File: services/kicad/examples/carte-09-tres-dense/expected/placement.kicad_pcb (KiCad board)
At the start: 2 copper layers, 130 x 100 mm, 62 parts, among them J1 IN_5V, J10 IO0, J11 IO1, J12 IO2, J13 IO3, J14 IO4, J2 SWD, U1 STM32F103C8T6, U2 AMS1117-3.3

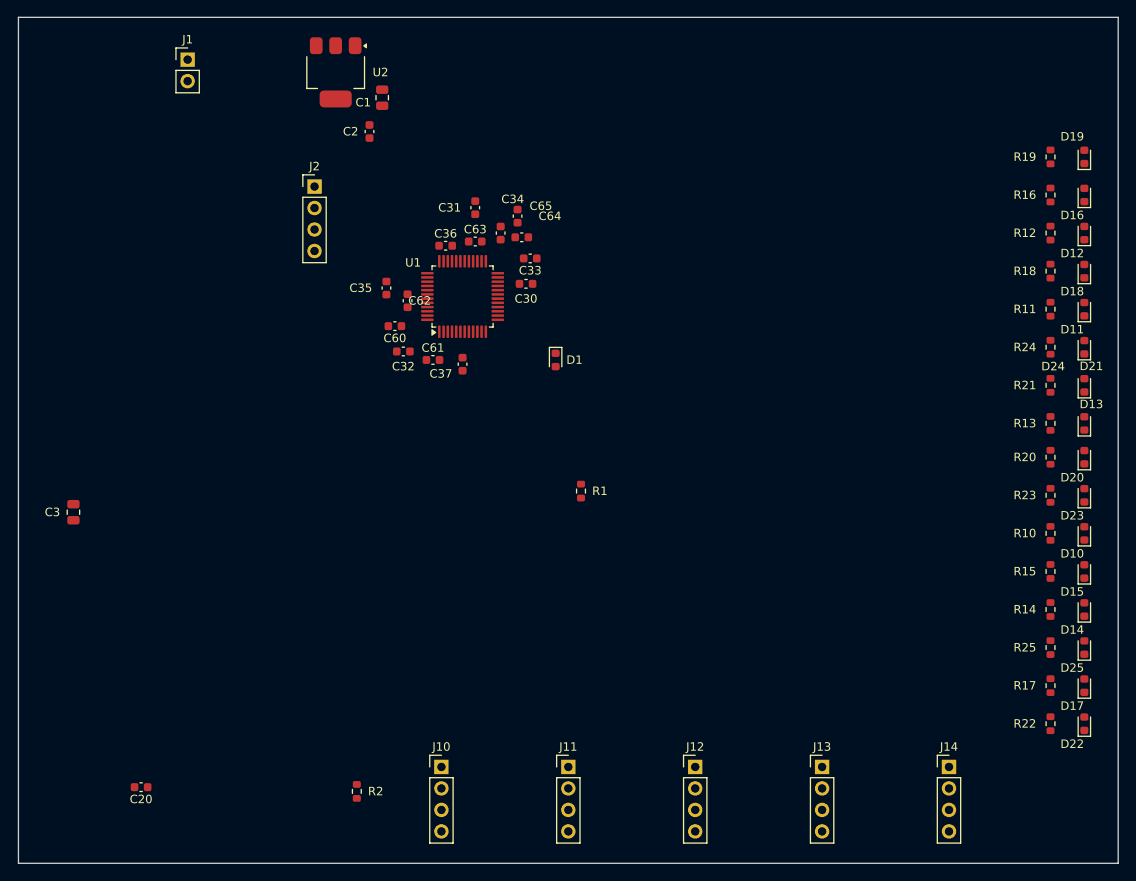
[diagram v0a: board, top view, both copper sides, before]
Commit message: feat(placement): les peripheriques se REPARTISSENT, ils ne s empilent plus
Question de l utilisateur devant le rendu : « c est quoi ce type de placement ? ».
Les composants s entassaient d un seul cote du boitier, etiquettes de
serigraphie l une sur l autre, trois quarts de la couronne vides.

TROIS CAUSES, toutes dans `_poser_les_peripheriques`, toutes la meme faute —
un angle unique pour tout un groupe :

  - les DIRECTS qui visent la meme broche (tous les decouplages d un rail,
    toutes les resistances d un meme signal) recevaient le MEME `angle_vers`
    et le meme rayon de depart ;
  - les SUIVEURS d un meme parent recevaient tous atan2(parent - centre) ;
  - les ISOLES partaient tous de l angle 0.0, c est-a-dire du meme point.

`le_long_du_rayon` ne s ecartait qu une fois la place prise : d ou la file.

REMEDE : `_ecart_en_eventail`. Le PREMIER de chaque groupe garde EXACTEMENT la
direction calculee — c est la topologie, on ne la perd pas pour faire joli — et
les suivants s ecartent symetriquement de 3 x `_PAS_ANGLE_DEG`.
Rien de deja pose ne bouge : seul l ANGLE DE DEPART de la recherche change, et
`le_long_du_rayon` reste seul juge de ce qui est libre.

BANC DES DIX CARTES, contour resserre ET peripheriques repartis :

    carte             demandee    livree         err  manq
    carte-01           25 x 20    20,1 x 13,6     0    0
    carte-02           55 x 40    34,9 x 25,2     0    0
    carte-03           50 x 35    27,6 x 19,9     0    0
    carte-04           60 x 45    36,6 x 29,8     0    0
    carte-05           70 x 50    40,0 x 32,6     0    0
    carte-06           80 x 60    46,5 x 36,4     0    0
    carte-07          110 x 80    47,7 x 38,8     0    0
    carte-08          125 x 95    57,4 x 44,1     0    0
    carte-09          130 x 100   57,8 x 45,2     0    0
    carte-10          140 x 105   59,0 x 45,8     0    0

Dix sur dix, 100 % route. carte-07 gagne 5,5 mm de largeur sur le passage
precedent, carte-06 deux, carte-10 deux. Sur ca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
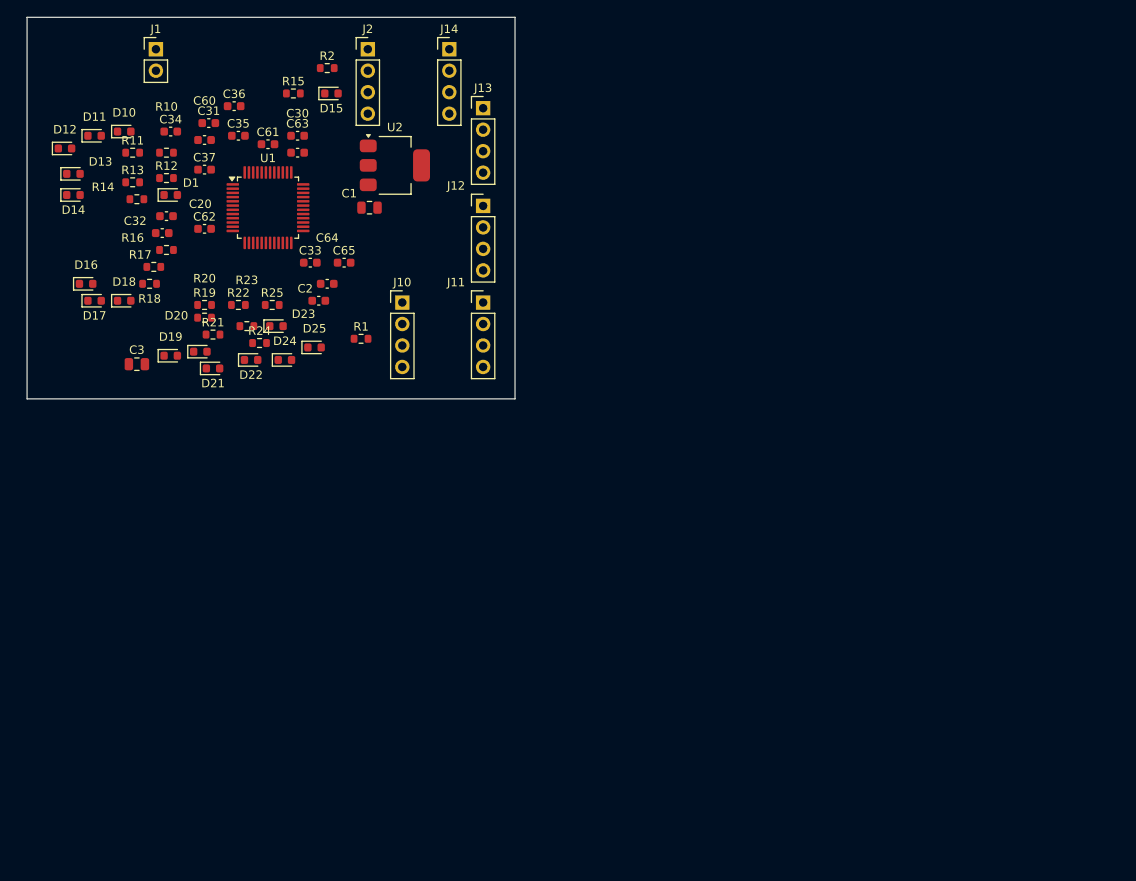
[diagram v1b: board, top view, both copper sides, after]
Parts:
- moved D14 129.2 mm to (90.0, 76.0), turned to 0 degrees
- moved D17 125.5 mm to (92.5, 88.5), turned to 0 degrees
- moved D13 123.1 mm to (90.0, 73.5), turned to 0 degrees
- moved D10 123.0 mm to (96.0, 68.5), turned to 0 degrees
- moved D12 120.9 mm to (89.0, 70.5), turned to 0 degrees
- moved D11 118.8 mm to (92.5, 69.0), turned to 0 degrees
- moved D16 118.5 mm to (91.5, 86.5), turned to 0 degrees
- moved R14 118.4 mm to (97.5, 76.5), turned to 0 degrees
- moved R17 117.0 mm to (99.5, 84.5), turned to 0 degrees
- moved R10 113.8 mm to (101.0, 71.0), turned to 0 degrees
- moved D18 113.6 mm to (96.0, 88.5), turned to 0 degrees
- moved R13 112.2 mm to (97.0, 74.5), turned to 0 degrees
- moved D19 110.5 mm to (101.5, 95.0), turned to 0 degrees
- moved R11 110.1 mm to (97.0, 71.0), turned to 0 degrees
- moved R22 108.0 mm to (109.5, 89.0), turned to 0 degrees
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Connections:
- U1 pad 36: Net-(U1-36) -> PWR_FLAG
- U1 pad 48: Net-(U1-48) -> PWR_FLAG
- U1 pad 9: IO_L5 -> PWR_FLAG
- U2 pad 3: VIN -> PWR_FLAG
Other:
- board size 130 x 100 mm -> 57.7 x 45.1 mm

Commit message: docs(banc): les dix boards du banc du 2026-09-23, service corrige
Artefacts du banc dont le tableau est deja commite : les dix cartes a
100 % route, 0 erreur, 0 connexion manquante, chacune a la taille de son
circuit.

Co-Authored-By: Claude Opus 5 <noreply@anthropic.com>
Claude-Session: https://claude.ai/code/session_01TnMqm4La2CxQHHB5K8aSSV
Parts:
- moved C36 15.0 mm to (105.0, 80.0)
- moved C34 14.1 mm to (105.5, 82.0)
- moved C63 13.2 mm to (103.5, 67.0)
- moved C32 11.5 mm to (101.0, 69.0)
- moved C31 10.6 mm to (116.0, 71.0)
- moved C62 10.5 mm to (105.5, 69.5)
- moved C64 9.51 mm to (110.5, 86.0)
- moved C30 3.64 mm to (113.0, 70.0)
- moved C60 3.64 mm to (109.0, 68.5)
- moved C65 3.20 mm to (120.0, 86.5)
- moved C35 3.04 mm to (110.0, 66.0)
- moved C61 2.06 mm to (112.5, 68.0)
- moved J12 1.00 mm to (138.4, 76.3)
- moved J13 1.00 mm to (138.4, 64.7)
- moved J11 0.87 mm to (138.4, 87.8)
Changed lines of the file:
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@@
 		(generator "kicad-footprint-generator")
 		(layer "F.Cu")
-		(at 116.5 71)
+		(at 113 70)
 		(descr "Capacitor SMD 0603 (1608 Metric), square (rectangular) end terminal, IPC-7351 nominal, (Body size source: IPC-SM-782 page 76, https://www.pcb-3d.com/wordpress/wp-content/uploads/ipc-sm-782a_amendment_1_and_2.pdf)")
 		(tags "capacitor")
 		(property "Reference" "C30"
-			(at -5.8783e-16 -4.63 0)
+			(at -2.82843 1.39843 0)
 			(layer "F.SilkS")
 			(effects
@@
 		(generator "kicad-footprint-generator")
 		(layer "F.Cu")
-		(at 106 67.5)
+		(at 116 71)
 		(descr "Capacitor SMD 0603 (1608 Metric), square (rectangular) end terminal, IPC-7351 nominal, (Body size source: IPC-SM-782 page 76, https://www.pcb-3d.com/wordpress/wp-content/uploads/ipc-sm-782a_amendment_1_and_2.pdf)")
 		(tags "capacitor")
@@
 		(generator "kicad-footprint-generator")
 		(layer "F.Cu")
-		(at 100.5 80.5)
+		(at 101 69)
 		(descr "Capacitor SMD 0603 (1608 Metric), square (rectangular) end terminal, IPC-7351 nominal, (Body size source: IPC-SM-782 page 76, https://www.pcb-3d.com/wordpress/wp-content/uploads/ipc-sm-782a_amendment_1_and_2.pdf)")
 		(tags "capacitor")
 		(property "Reference" "C32"
-			(at -3.2 -1.43 0)
+			(at -0.8 -1.43 0)
 			(layer "F.SilkS")
 			(effects
@@
 		(generator "kicad-footprint-generator")
 		(layer "F.Cu")
-		(at 101.5 68.5)
+		(at 105.5 82)
 		(descr "Capacitor SMD 0603 (1608 Metric), square (rectangular) end terminal, IPC-7351 nominal, (Body size source: IPC-SM-782 page 76, https://www.pcb-3d.com/wordpress/wp-content/uploads/ipc-sm-782a_amendment_1_and_2.pdf)")
 		(tags "capacitor")
 		(property "Reference" "C34"
-			(at 0 -1.43 0)
+			(at 1.95943e-16 1.77 0)
 			(layer "F.SilkS")
 			(effects
@@
 		(generator "kicad-footprint-generator")
 		(layer "F.Cu")
-		(at 109.5 69)
+		(at 110 66)
 		(descr "Capacitor SMD 0603 (1608 Metric), square (rectangular) end terminal, IPC-7351 nominal, (Body size source: IPC-SM-782 page 76, https://www.pcb-3d.com/wordpress/wp-content/uploads/ipc-sm-782a_amendment_1_and_2.pdf)")
 		(tags "capacitor")
@@
 		(generator "kicad-footprint-generator")
 		(layer "F.Cu")
-		(at 109 65.5)
+		(at 105 80)
 		(descr "Capacitor SMD 0603 (1608 Metric), square (rectangular) end terminal, IPC-7351 nominal, (Body size source: IPC-SM-782 page 76, https://www.pcb-3d.com/wordpress/wp-content/uploads/ipc-sm-782a_amendment_1_and_2.pdf)")
 		(tags "capacitor")
@@
 		(tags "resistor")
 		(property "Reference" "R10"
-			(at -7.34788e-16 -5.43 0)
+			(at 0 -1.43 0)
 			(layer "F.SilkS")
 			(effects
@@
 		(tags "resistor")
 		(property "Reference" "R14"
-			(at -4 -1.43 0)
+			(at 1.95943e-16 1.77 0)
 			(layer "F.SilkS")
 			(effects
@@
 		(tags "resistor")
 		(property "Reference" "R16"
-			(at -4 -1.43 0)
+			(at 0 -1.43 0)
 			(layer "F.SilkS")
 			(effects
@@
 		(tags "resistor")
 		(property "Reference" "R23"
-			(at -7.34788e-16 -5.43 0)
+			(at 0 -1.43 0)
 			(layer "F.SilkS")
 			(effects
@@
 		(generator "kicad-footprint-generator")
 		(layer "F.Cu")
-		(at 138.43 88.71)
+		(at 138.43 87.8421)
 		(descr "Through hole straight pin header, 1x04, 2.54mm pitch, single row")
 		(tags "Through hole pin header THT 1x04 2.54mm single row")
@@
 		(generator "kicad-footprint-generator")
 		(layer "F.Cu")
-		(at 138.43 77.2911)
+		(at 138.43 76.2911)
 		(descr "Through hole straight pin header, 1x04, 2.54mm pitch, single row")
 		(tags "Through hole pin header THT 1x04 2.54mm single row")
@@
 		(generator "kicad-footprint-generator")
 		(layer "F.Cu")
-		(at 138.43 65.74)
+		(at 138.43 64.74)
 		(descr "Through hole straight pin header, 1x04, 2.54mm pitch, single row")
 		(tags "Through hole pin header THT 1x04 2.54mm single row")
@@
 		(generator "kicad-footprint-generator")
 		(layer "F.Cu")
-		(at 105.5 69.5)
+		(at 109 68.5)
 		(descr "Capacitor SMD 0603 (1608 Metric), square (rectangular) end terminal, IPC-7351 nominal, (Body size source: IPC-SM-782 page 76, https://www.pcb-3d.com/wordpress/wp-content/uploads/ipc-sm-782a_amendment_1_and_2.pdf)")
 		(tags "capacitor")
 		(property "Reference" "C60"
-			(at -5.8783e-16 -4.63 0)
+			(at -7.34788e-16 -5.43 0)
 			(layer "F.SilkS")
 			(effects
@@
 		(generator "kicad-footprint-generator")
 		(layer "F.Cu")
-		(at 113 70)
+		(at 112.5 68)
 		(descr "Capacitor SMD 0603 (1608 Metric), square (rectangular) end terminal, IPC-7351 nominal, (Body size source: IPC-SM-782 page 76, https://www.pcb-3d.com/wordpress/wp-content/uploads/ipc-sm-782a_amendment_1_and_2.pdf)")
 		(tags "capacitor")
 		(property "Reference" "C61"
-			(at 0 -1.43 0)
+			(at 0.8 -1.43 0)
 			(layer "F.SilkS")
 			(effects
@@
 		(generator "kicad-footprint-generator")
 		(layer "F.Cu")
-		(at 105.5 80)
+		(at 105.5 69.5)
 		(descr "Capacitor SMD 0603 (1608 Metric), square (rectangular) end terminal, IPC-7351 nominal, (Body size source: IPC-SM-782 page 76, https://www.pcb-3d.com/wordpress/wp-content/uploads/ipc-sm-782a_amendment_1_and_2.pdf)")
 		(tags "capacitor")
 		(property "Reference" "C62"
-			(at 0 -1.43 0)
+			(at 1.13137 -2.56137 0)
 			(layer "F.SilkS")
 			(effects
@@
 		(generator "kicad-footprint-generator")
 		(layer "F.Cu")
-		(at 116.5 69)
+		(at 103.5 67)
 		(descr "Capacitor SMD 0603 (1608 Metric), square (rectangular) end terminal, IPC-7351 nominal, (Body size source: IPC-SM-782 page 76, https://www.pcb-3d.com/wordpress/wp-content/uploads/ipc-sm-782a_amendment_1_and_2.pdf)")
 		(tags "capacitor")
@@
 		(generator "kicad-footprint-generator")
 		(layer "F.Cu")
-		(at 120 86.5)
+		(at 110.5 86)
 		(descr "Capacitor SMD 0603 (1608 Metric), square (rectangular) end terminal, IPC-7351 nominal, (Body size source: IPC-SM-782 page 76, https://www.pcb-3d.com/wordpress/wp-content/uploads/ipc-sm-782a_amendment_1_and_2.pdf)")
 		(tags "capacitor")
 		(property "Reference" "C64"
-			(at -7.34788e-16 -5.43 0)
+			(at 0 -1.43 0)
 			(layer "F.SilkS")
 			(effects
@@
 		(generator "kicad-footprint-generator")
 		(layer "F.Cu")
-		(at 122 84)
+		(at 120 86.5)
 		(descr "Capacitor SMD 0603 (1608 Metric), square (rectangular) end terminal, IPC-7351 nominal, (Body size source: IPC-SM-782 page 76, https://www.pcb-3d.com/wordpress/wp-content/uploads/ipc-sm-782a_amendment_1_and_2.pdf)")
 		(tags "capacitor")
 		(property "Reference" "C65"
-			(at 0 -1.43 0)
+			(at 1.6 -1.43 0)
 			(layer "F.SilkS")
 			(effects

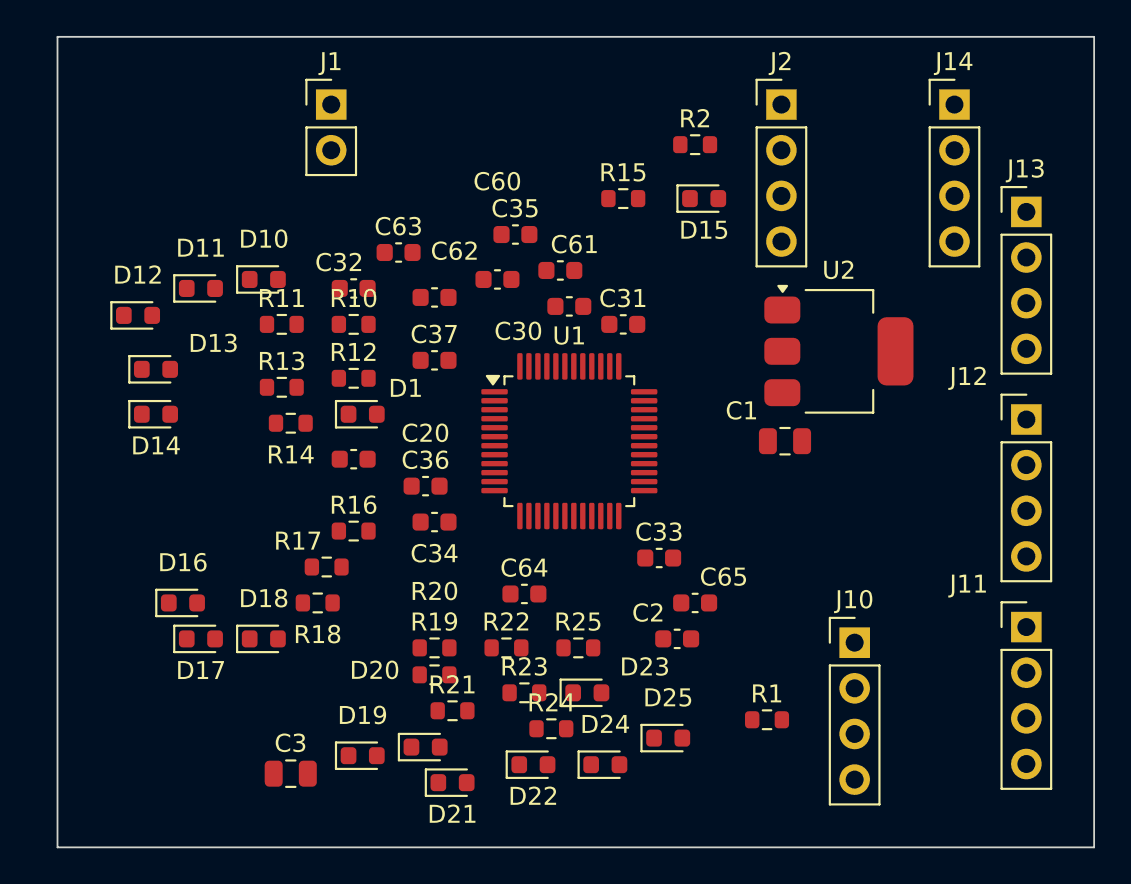
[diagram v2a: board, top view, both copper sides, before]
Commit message: fix(banc): le banc route comme la production — plafond 8, budget du client
D-2026-09-24-f. run_pipeline.py prenait 2 couches et 1800 s par défaut, et
carte-07 écrivait 2 en dur : dix cartes sur quinze ne pouvaient jamais
escalader, et la règle « toute connexion manquante fait monter » était
inerte dans le banc. Mesuré sur carte-07 : 97 %, seule la masse manquante,
« le palier suivant sera tenté »… puis retour à 2 couches.

Plafond par défaut 8 (client Pro Max), budget min(600 + 300 x plafond, 3600)
comme routingSearchBudgetS côté client. En production, rien ne change : le
plafond reste celui du plan.

Livraisons du jour, toutes vérifiées par kicad-cli et contre le schéma
(0 erreur bloquante, 0 connexion manquante, 0 court-circuit) :
carte-04, 05, 06, 08 (campagne de l'après-midi) et carte-09, 10 (4 couches).
Les boards versionnés de ces cartes court-circuitaient des nets du schéma.

Correction de ma propre erreur dans la doc : carte-07 n'avait jamais
escaladé ; les lignes « palier 4 et 6 » du journal étaient celles de
carte-08, démarrée la même minute.

Co-Authored-By: Claude Opus 5.5 <noreply@anthropic.com>
Claude-Session: https://claude.ai/code/session_01TnMqm4La2CxQHHB5K8aSSV
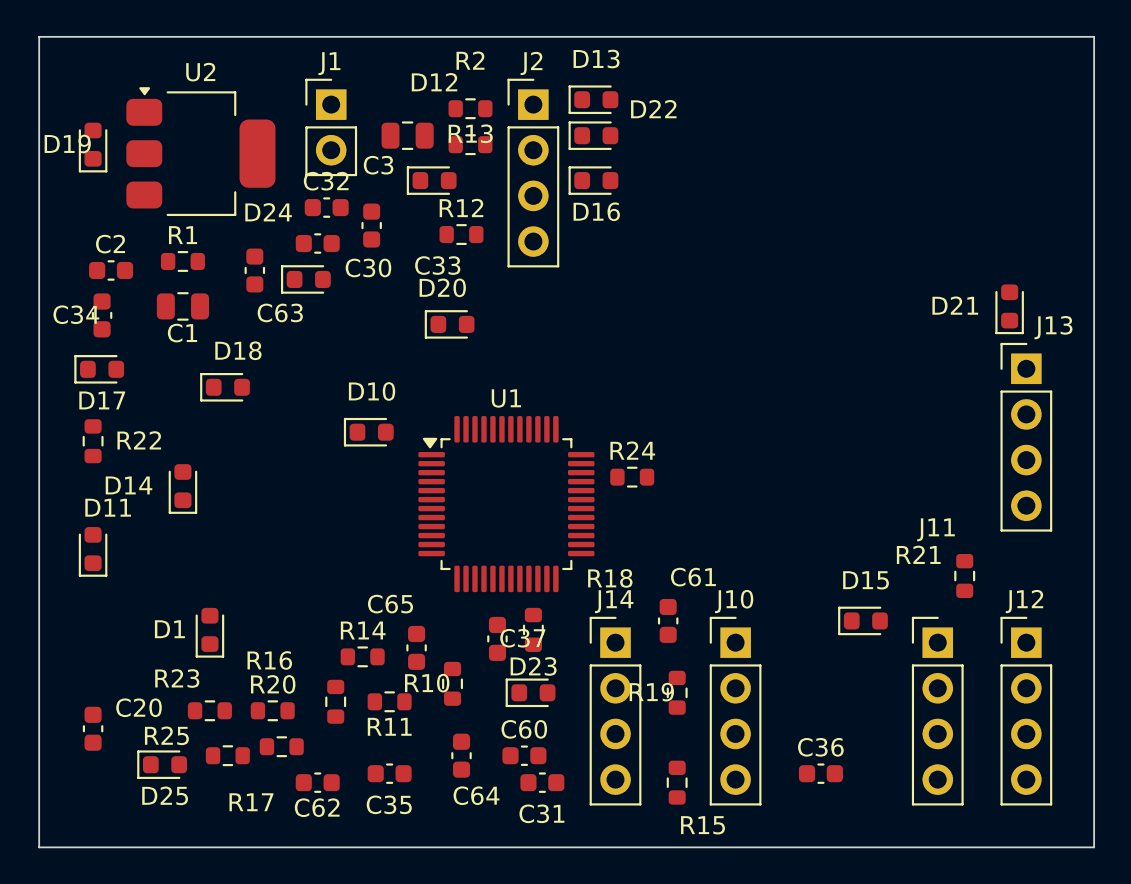
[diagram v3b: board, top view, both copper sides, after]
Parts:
- moved R1 41.3 mm to (91.5, 67.5)
- moved D21 40.8 mm to (137.5, 70.0), turned to 90 degrees
- moved C2 37.6 mm to (87.5, 68.0)
- moved U2 37.2 mm to (92.5, 61.5)
- moved D19 37.2 mm to (86.5, 61.0), turned to 90 degrees
- moved C3 36.1 mm to (104.0, 60.5), turned to 180 degrees
- moved J14 35.4 mm to (115.6, 88.7)
- moved D22 35.2 mm to (114.5, 60.5)
- moved C1 34.3 mm to (91.5, 70.0)
- moved D16 32.9 mm to (114.5, 63.0)
- moved R15 32.6 mm to (119.0, 96.5), turned to 270 degrees
- moved D24 31.6 mm to (98.5, 68.5)
- moved C35 30.8 mm to (103.0, 96.0)
- moved R21 29.5 mm to (135.0, 85.0), turned to 90 degrees
- moved D13 28.7 mm to (114.5, 58.5)
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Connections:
- C3 pad 1: Net-(C3-1) -> +3V3
- U1 pad 36: PWR_FLAG -> +3V3
- U1 pad 48: PWR_FLAG -> +3V3
- U1 pad 9: PWR_FLAG -> IO_L5
- U2 pad 2: Net-(U2-2) -> +3V3
- U2 pad 3: PWR_FLAG -> VIN
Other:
- board size 57.7 x 45.1 mm -> 58.7 x 45.1 mm
